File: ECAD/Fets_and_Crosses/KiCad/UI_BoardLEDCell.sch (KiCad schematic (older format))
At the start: 20 parts, among them Q1321 2N7002, Q1322 2N7002

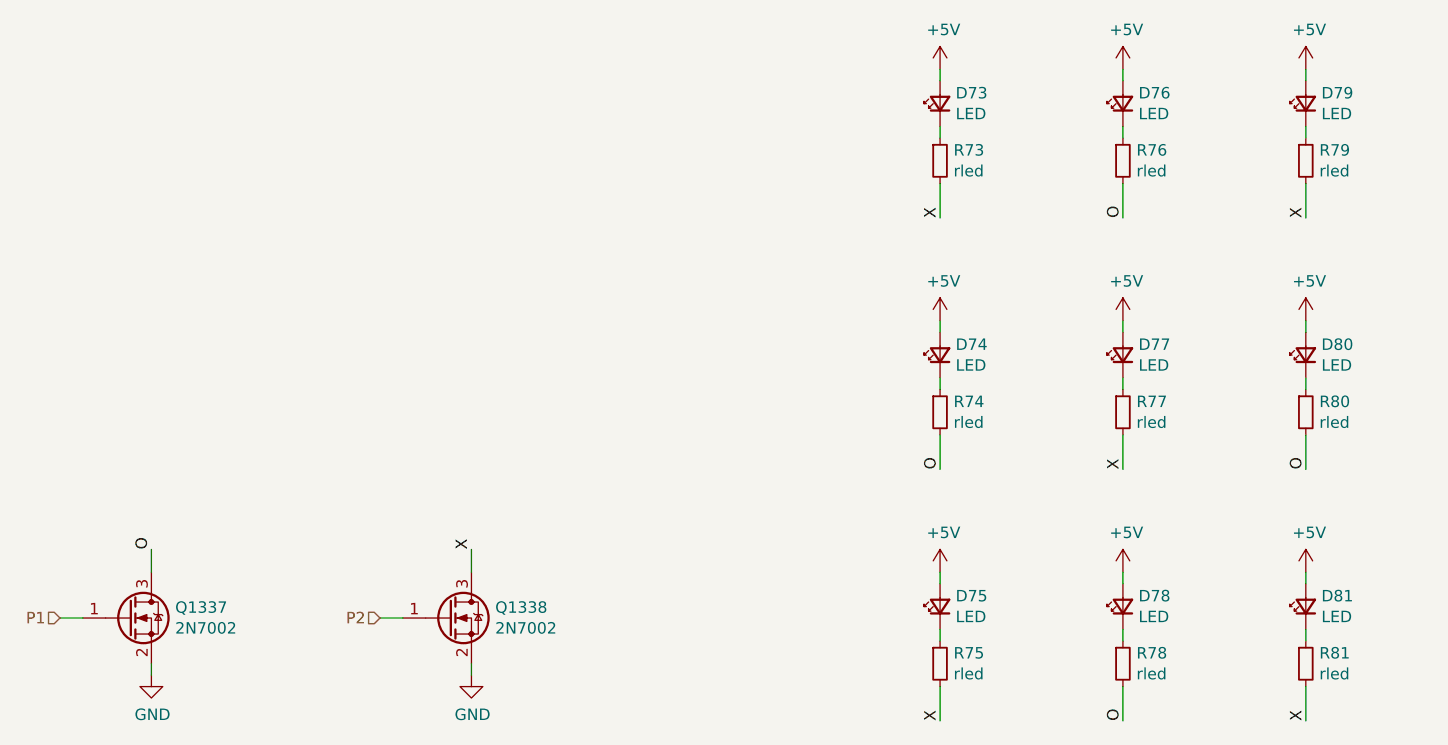
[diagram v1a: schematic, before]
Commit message: Seperated Red/Green LEDs
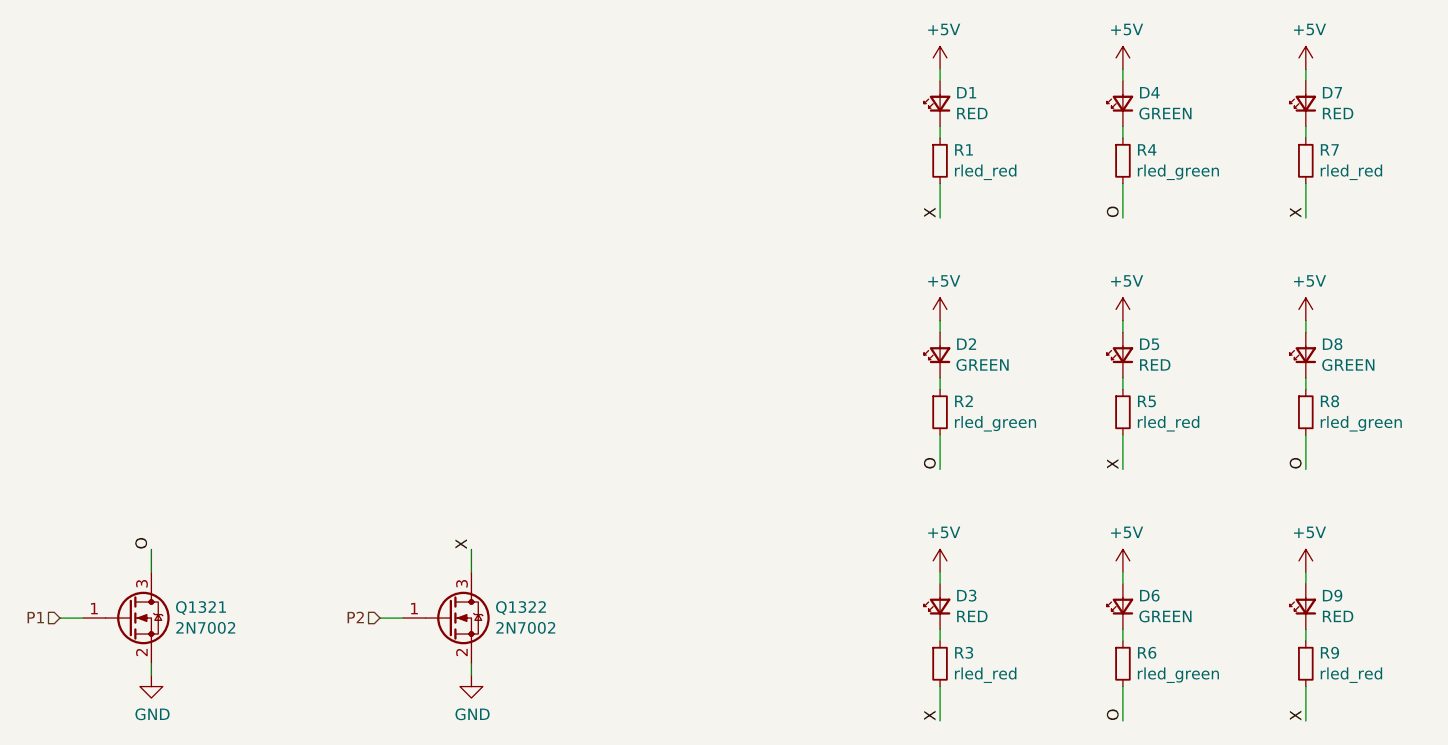
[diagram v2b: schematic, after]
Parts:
- D1, D3, D5, D7, D9: value LED -> RED
- D2, D4, D6, D8: value LED -> GREEN
- R1, R3, R5, R7, R9: value rled -> rled_red
- R2, R4, R6, R8: value rled -> rled_green

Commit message: Added Most LCSC Part Numbers
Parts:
- D1, D3, D5, D7, D9: LCSC (none) -> C72037
- D2, D4, D6, D8: LCSC (none) -> C84260
- Q1321, Q1322: LCSC (none) -> C8545
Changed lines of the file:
@@
 F 2 "LogicQ:D_0805_2012Metric_NOLBL" V 6350 2450 50  0001 C CNN
 F 3 "~" V 6350 2450 50  0001 C CNN
+F 4 "C72037" H 6350 2450 50  0001 C CNN "LCSC"
 	1    6350 2450
 	0    -1   -1   0
@@
 AR Path="/5E53AD22/5E56E945/5E5529CD" Ref="#PWR01010"  Part="1"
 AR Path="/5E53AD22/5E56E949/5E5529CD" Ref="#PWR01021"  Part="1"
-F 0 "#PWR0933" H 6350 2150 50  0001 C CNN
+F 0 "#PWR01021" H 6350 2150 50  0001 C CNN
 F 1 "+5V" H 6365 2473 50  0000 C CNN
 F 2 "" H 6350 2300 50  0001 C CNN
@@
 F 2 "LogicQ:D_0805_2012Metric_NOLBL" V 7150 2450 50  0001 C CNN
 F 3 "~" V 7150 2450 50  0001 C CNN
+F 4 "C84260" H 7150 2450 50  0001 C CNN "LCSC"
 	1    7150 2450
 	0    -1   -1   0
@@
 AR Path="/5E53AD22/5E56E945/5E55850F" Ref="#PWR01011"  Part="1"
 AR Path="/5E53AD22/5E56E949/5E55850F" Ref="#PWR01022"  Part="1"
-F 0 "#PWR0934" H 7150 2150 50  0001 C CNN
+F 0 "#PWR01022" H 7150 2150 50  0001 C CNN
 F 1 "+5V" H 7165 2473 50  0000 C CNN
 F 2 "" H 7150 2300 50  0001 C CNN
@@
 F 2 "LogicQ:D_0805_2012Metric_NOLBL" V 7950 2450 50  0001 C CNN
 F 3 "~" V 7950 2450 50  0001 C CNN
+F 4 "C72037" H 7950 2450 50  0001 C CNN "LCSC"
 	1    7950 2450
 	0    -1   -1   0
@@
 AR Path="/5E53AD22/5E56E945/5E5596E4" Ref="#PWR01012"  Part="1"
 AR Path="/5E53AD22/5E56E949/5E5596E4" Ref="#PWR01023"  Part="1"
-F 0 "#PWR0935" H 7950 2150 50  0001 C CNN
+F 0 "#PWR01023" H 7950 2150 50  0001 C CNN
 F 1 "+5V" H 7965 2473 50  0000 C CNN
 F 2 "" H 7950 2300 50  0001 C CNN
@@
 F 2 "LogicQ:D_0805_2012Metric_NOLBL" V 6350 3550 50  0001 C CNN
 F 3 "~" V 6350 3550 50  0001 C CNN
+F 4 "C84260" H 6350 3550 50  0001 C CNN "LCSC"
 	1    6350 3550
 	0    -1   -1   0
@@
 AR Path="/5E53AD22/5E56E945/5E55E05C" Ref="#PWR01013"  Part="1"
 AR Path="/5E53AD22/5E56E949/5E55E05C" Ref="#PWR01024"  Part="1"
-F 0 "#PWR0936" H 6350 3250 50  0001 C CNN
+F 0 "#PWR01024" H 6350 3250 50  0001 C CNN
 F 1 "+5V" H 6365 3573 50  0000 C CNN
 F 2 "" H 6350 3400 50  0001 C CNN
@@
 F 2 "LogicQ:D_0805_2012Metric_NOLBL" V 7150 3550 50  0001 C CNN
 F 3 "~" V 7150 3550 50  0001 C CNN
+F 4 "C72037" H 7150 3550 50  0001 C CNN "LCSC"
 	1    7150 3550
 	0    -1   -1   0
@@
 AR Path="/5E53AD22/5E56E945/5E55E071" Ref="#PWR01014"  Part="1"
 AR Path="/5E53AD22/5E56E949/5E55E071" Ref="#PWR01025"  Part="1"
-F 0 "#PWR0937" H 7150 3250 50  0001 C CNN
+F 0 "#PWR01025" H 7150 3250 50  0001 C CNN
 F 1 "+5V" H 7165 3573 50  0000 C CNN
 F 2 "" H 7150 3400 50  0001 C CNN
@@
 F 2 "LogicQ:D_0805_2012Metric_NOLBL" V 7950 3550 50  0001 C CNN
 F 3 "~" V 7950 3550 50  0001 C CNN
+F 4 "C84260" H 7950 3550 50  0001 C CNN "LCSC"
 	1    7950 3550
 	0    -1   -1   0
@@
 AR Path="/5E53AD22/5E56E945/5E55E086" Ref="#PWR01015"  Part="1"
 AR Path="/5E53AD22/5E56E949/5E55E086" Ref="#PWR01026"  Part="1"
-F 0 "#PWR0938" H 7950 3250 50  0001 C CNN
+F 0 "#PWR01026" H 7950 3250 50  0001 C CNN
 F 1 "+5V" H 7965 3573 50  0000 C CNN
 F 2 "" H 7950 3400 50  0001 C CNN
@@
 F 2 "LogicQ:D_0805_2012Metric_NOLBL" V 6350 4650 50  0001 C CNN
 F 3 "~" V 6350 4650 50  0001 C CNN
+F 4 "C72037" H 6350 4650 50  0001 C CNN "LCSC"
 	1    6350 4650
 	0    -1   -1   0
@@
 AR Path="/5E53AD22/5E56E945/5E56770C" Ref="#PWR01016"  Part="1"
 AR Path="/5E53AD22/5E56E949/5E56770C" Ref="#PWR01027"  Part="1"
-F 0 "#PWR0939" H 6350 4350 50  0001 C CNN
+F 0 "#PWR01027" H 6350 4350 50  0001 C CNN
 F 1 "+5V" H 6365 4673 50  0000 C CNN
 F 2 "" H 6350 4500 50  0001 C CNN
@@
 F 2 "LogicQ:D_0805_2012Metric_NOLBL" V 7150 4650 50  0001 C CNN
 F 3 "~" V 7150 4650 50  0001 C CNN
+F 4 "C84260" H 7150 4650 50  0001 C CNN "LCSC"
 	1    7150 4650
 	0    -1   -1   0
@@
 AR Path="/5E53AD22/5E56E945/5E567721" Ref="#PWR01017"  Part="1"
 AR Path="/5E53AD22/5E56E949/5E567721" Ref="#PWR01028"  Part="1"
-F 0 "#PWR0940" H 7150 4350 50  0001 C CNN
+F 0 "#PWR01028" H 7150 4350 50  0001 C CNN
 F 1 "+5V" H 7165 4673 50  0000 C CNN
 F 2 "" H 7150 4500 50  0001 C CNN
@@
 F 2 "LogicQ:D_0805_2012Metric_NOLBL" V 7950 4650 50  0001 C CNN
 F 3 "~" V 7950 4650 50  0001 C CNN
+F 4 "C72037" H 7950 4650 50  0001 C CNN "LCSC"
 	1    7950 4650
 	0    -1   -1   0
@@
 AR Path="/5E53AD22/5E56E945/5E567736" Ref="#PWR01018"  Part="1"
 AR Path="/5E53AD22/5E56E949/5E567736" Ref="#PWR01029"  Part="1"
-F 0 "#PWR0941" H 7950 4350 50  0001 C CNN
+F 0 "#PWR01029" H 7950 4350 50  0001 C CNN
 F 1 "+5V" H 7965 4673 50  0000 C CNN
 F 2 "" H 7950 4500 50  0001 C CNN
@@
 F 2 "LogicQ:SOT-23-N" H 3000 4800 50  0001 C CNN
 F 3 "~" H 2800 4700 50  0001 C CNN
+F 4 "C8545" H 2800 4700 50  0001 C CNN "LCSC"
 	1    2800 4700
 	1    0    0    -1
@@
 F 2 "LogicQ:SOT-23-N" H 4400 4800 50  0001 C CNN
 F 3 "~" H 4200 4700 50  0001 C CNN
+F 4 "C8545" H 4200 4700 50  0001 C CNN "LCSC"
 	1    4200 4700
 	1    0    0    -1
@@
 AR Path="/5E53AD22/5E56E945/5E55F52F" Ref="#PWR01019"  Part="1"
 AR Path="/5E53AD22/5E56E949/5E55F52F" Ref="#PWR01030"  Part="1"
-F 0 "#PWR0942" H 2900 4700 50  0001 C CNN
+F 0 "#PWR01030" H 2900 4700 50  0001 C CNN
 F 1 "GND" H 2905 4777 50  0000 C CNN
 F 2 "" H 2900 4950 50  0001 C CNN
@@
 AR Path="/5E53AD22/5E56E945/5E561894" Ref="#PWR01020"  Part="1"
 AR Path="/5E53AD22/5E56E949/5E561894" Ref="#PWR01031"  Part="1"
-F 0 "#PWR0943" H 4300 4700 50  0001 C CNN
+F 0 "#PWR01031" H 4300 4700 50  0001 C CNN
 F 1 "GND" H 4305 4777 50  0000 C CNN
 F 2 "" H 4300 4950 50  0001 C CNN

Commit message: Specified LED Resisitors
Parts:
- R1, R3, R5, R7, R9: value rled_red -> 1K; LCSC (none) -> C21190
- R2, R4, R6, R8: value rled_green -> 20K; LCSC (none) -> C4184
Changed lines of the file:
@@
 AR Path="/5E53AD22/5E56E949/5E552463" Ref="R73"  Part="1"
 F 0 "R1" H 6409 2746 50  0000 L CNN
-F 1 "rled_red" H 6409 2655 50  0000 L CNN
+F 1 "1K" H 6409 2655 50  0000 L CNN
 F 2 "LogicQ:R_0603_1608Metric_NOLBL" H 6350 2700 50  0001 C CNN
 F 3 "~" H 6350 2700 50  0001 C CNN
+F 4 "C21190" H 6350 2700 50  0001 C CNN "LCSC"
 	1    6350 2700
 	1    0    0    -1
@@
 AR Path="/5E53AD22/5E56E949/5E558508" Ref="R76"  Part="1"
 F 0 "R4" H 7209 2746 50  0000 L CNN
-F 1 "rled_green" H 7209 2655 50  0000 L CNN
+F 1 "20K" H 7209 2655 50  0000 L CNN
 F 2 "LogicQ:R_0603_1608Metric_NOLBL" H 7150 2700 50  0001 C CNN
 F 3 "~" H 7150 2700 50  0001 C CNN
+F 4 "C4184" H 7150 2700 50  0001 C CNN "LCSC"
 	1    7150 2700
 	1    0    0    -1
@@
 AR Path="/5E53AD22/5E56E949/5E5596DD" Ref="R79"  Part="1"
 F 0 "R7" H 8009 2746 50  0000 L CNN
-F 1 "rled_red" H 8009 2655 50  0000 L CNN
+F 1 "1K" H 8009 2655 50  0000 L CNN
 F 2 "LogicQ:R_0603_1608Metric_NOLBL" H 7950 2700 50  0001 C CNN
 F 3 "~" H 7950 2700 50  0001 C CNN
+F 4 "C21190" H 7950 2700 50  0001 C CNN "LCSC"
 	1    7950 2700
 	1    0    0    -1
@@
 AR Path="/5E53AD22/5E56E949/5E55E055" Ref="R74"  Part="1"
 F 0 "R2" H 6409 3846 50  0000 L CNN
-F 1 "rled_green" H 6409 3755 50  0000 L CNN
+F 1 "20K" H 6409 3755 50  0000 L CNN
 F 2 "LogicQ:R_0603_1608Metric_NOLBL" H 6350 3800 50  0001 C CNN
 F 3 "~" H 6350 3800 50  0001 C CNN
+F 4 "C4184" H 6350 3800 50  0001 C CNN "LCSC"
 	1    6350 3800
 	1    0    0    -1
@@
 AR Path="/5E53AD22/5E56E949/5E55E06A" Ref="R77"  Part="1"
 F 0 "R5" H 7209 3846 50  0000 L CNN
-F 1 "rled_red" H 7209 3755 50  0000 L CNN
+F 1 "1K" H 7209 3755 50  0000 L CNN
 F 2 "LogicQ:R_0603_1608Metric_NOLBL" H 7150 3800 50  0001 C CNN
 F 3 "~" H 7150 3800 50  0001 C CNN
+F 4 "C21190" H 7150 3800 50  0001 C CNN "LCSC"
 	1    7150 3800
 	1    0    0    -1
@@
 AR Path="/5E53AD22/5E56E949/5E55E07F" Ref="R80"  Part="1"
 F 0 "R8" H 8009 3846 50  0000 L CNN
-F 1 "rled_green" H 8009 3755 50  0000 L CNN
+F 1 "20K" H 8009 3755 50  0000 L CNN
 F 2 "LogicQ:R_0603_1608Metric_NOLBL" H 7950 3800 50  0001 C CNN
 F 3 "~" H 7950 3800 50  0001 C CNN
+F 4 "C4184" H 7950 3800 50  0001 C CNN "LCSC"
 	1    7950 3800
 	1    0    0    -1
@@
 AR Path="/5E53AD22/5E56E949/5E567705" Ref="R75"  Part="1"
 F 0 "R3" H 6409 4946 50  0000 L CNN
-F 1 "rled_red" H 6409 4855 50  0000 L CNN
+F 1 "1K" H 6409 4855 50  0000 L CNN
 F 2 "LogicQ:R_0603_1608Metric_NOLBL" H 6350 4900 50  0001 C CNN
 F 3 "~" H 6350 4900 50  0001 C CNN
+F 4 "C21190" H 6350 4900 50  0001 C CNN "LCSC"
 	1    6350 4900
 	1    0    0    -1
@@
 AR Path="/5E53AD22/5E56E949/5E56771A" Ref="R78"  Part="1"
 F 0 "R6" H 7209 4946 50  0000 L CNN
-F 1 "rled_green" H 7209 4855 50  0000 L CNN
+F 1 "20K" H 7209 4855 50  0000 L CNN
 F 2 "LogicQ:R_0603_1608Metric_NOLBL" H 7150 4900 50  0001 C CNN
 F 3 "~" H 7150 4900 50  0001 C CNN
+F 4 "C4184" H 7150 4900 50  0001 C CNN "LCSC"
 	1    7150 4900
 	1    0    0    -1
@@
 AR Path="/5E53AD22/5E56E949/5E56772F" Ref="R81"  Part="1"
 F 0 "R9" H 8009 4946 50  0000 L CNN
-F 1 "rled_red" H 8009 4855 50  0000 L CNN
+F 1 "1K" H 8009 4855 50  0000 L CNN
 F 2 "LogicQ:R_0603_1608Metric_NOLBL" H 7950 4900 50  0001 C CNN
 F 3 "~" H 7950 4900 50  0001 C CNN
+F 4 "C21190" H 7950 4900 50  0001 C CNN "LCSC"
 	1    7950 4900
 	1    0    0    -1
